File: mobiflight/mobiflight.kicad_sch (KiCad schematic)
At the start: 24 parts, among them J1 Barrel_Jack_Switch, U1 ULN2003, U2 ULN2003, U3 ULN2003, U4 ULN2003, U5 ULN2003, U6 ULN2003

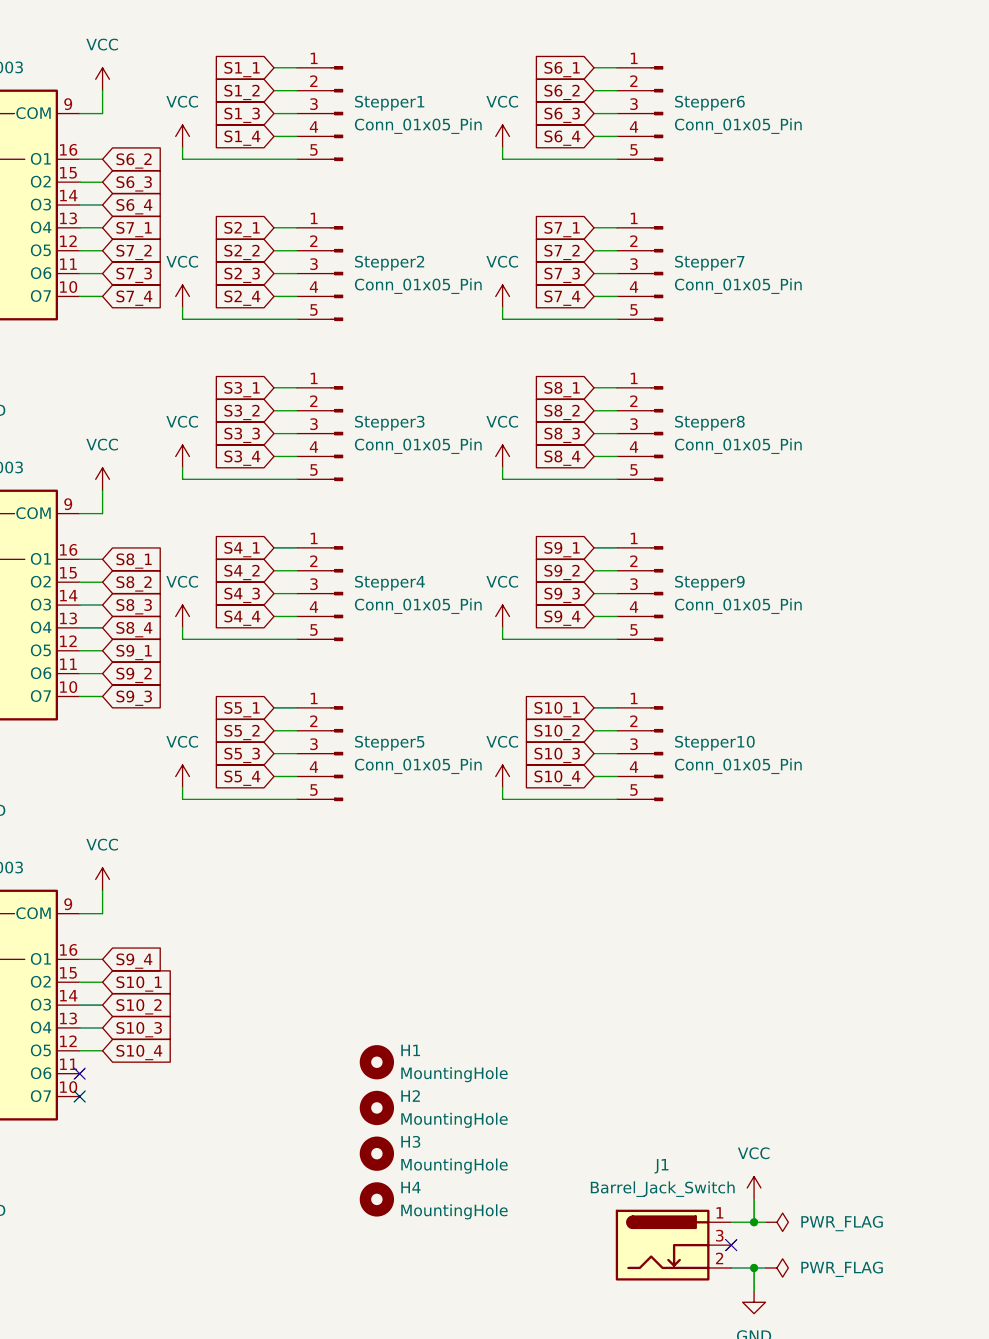
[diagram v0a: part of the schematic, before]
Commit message: add LEDs, move to SMD
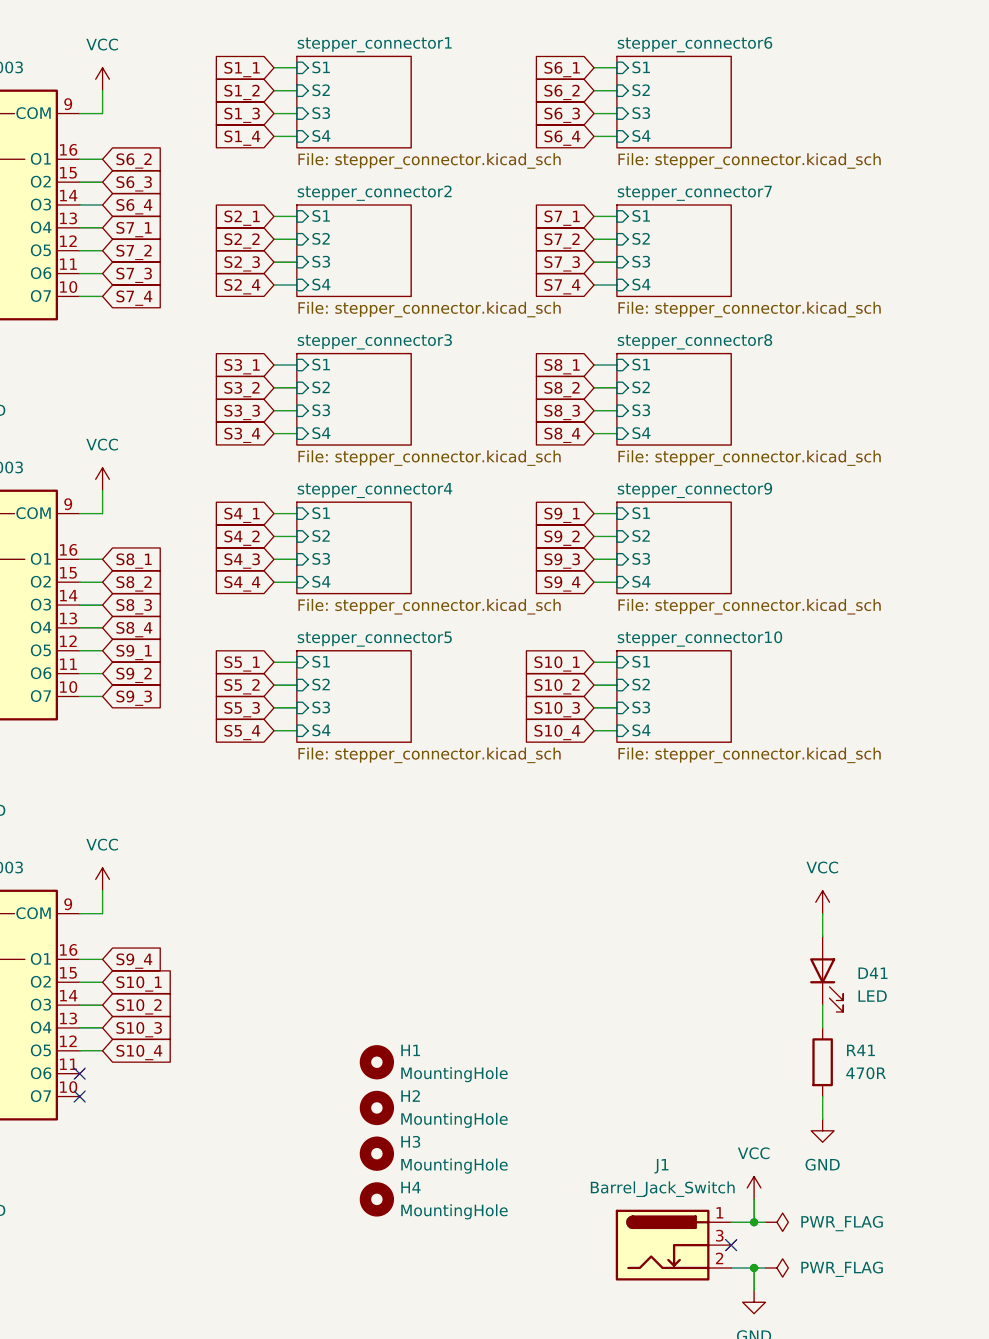
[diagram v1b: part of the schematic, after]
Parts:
- removed Stepper1, Stepper10, Stepper2, Stepper3, Stepper4, Stepper5, Stepper6, Stepper7, Stepper8, Stepper9: Conn_01x05_Pin, Connector_JST:JST_XH_B5B-XH-A_1x05_P2.50mm_Vertical, symbol Connector:Conn_01x05_Pin
- added D41: LED, LED_SMD:LED_0201_0603Metric, symbol Device:LED
- added R41: 470R, Resistor_SMD:R_0201_0603Metric, symbol Device:R
- U1, U2, U3, U4, U5, U6: footprint Package_DIP:DIP-16_W7.62mm_Socket_LongPads -> Package_SO:SOIC-16_3.9x9.9mm_P1.27mm
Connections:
- net GND: now also R41.2
- net VCC: now also D41.2 (A)
- new net: D41.1 (K), R41.1
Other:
- added sheet stepper_connector1 (stepper_connector.kicad_sch)
- added sheet stepper_connector10 (stepper_connector.kicad_sch)
- added sheet stepper_connector2 (stepper_connector.kicad_sch)
- added sheet stepper_connector3 (stepper_connector.kicad_sch)
- added sheet stepper_connector4 (stepper_connector.kicad_sch)
- added sheet stepper_connector5 (stepper_connector.kicad_sch)
- added sheet stepper_connector6 (stepper_connector.kicad_sch)
- added sheet stepper_connector7 (stepper_connector.kicad_sch)
- added sheet stepper_connector8 (stepper_connector.kicad_sch)
- added sheet stepper_connector9 (stepper_connector.kicad_sch)

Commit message: replace components
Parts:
- renumbered D41 to D1, R41 to R1
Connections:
- net D10: now also U1.1 (I1); no longer U1.7 (I7)
- net D11: now also U2.7 (I7); no longer U2.1 (I1)
- net D12: now also U2.6 (I6); no longer U2.2 (I2)
- net D13: now also U2.5 (I5); no longer U2.3 (I3)
- net D15: now also U2.3 (I3); no longer U2.5 (I5)
- net D16: now also U2.2 (I2); no longer U2.6 (I6)
- net D17: now also U2.1 (I1); no longer U2.7 (I7)
- net D18: now also U3.7 (I7); no longer U3.1 (I1)
- net D19: now also U3.6 (I6); no longer U3.2 (I2)
- net D20: now also U3.5 (I5); no longer U3.3 (I3)
- net D22: now also U3.3 (I3); no longer U3.5 (I5)
- net D23: now also U3.2 (I2); no longer U3.6 (I6)
- net D24: now also U3.1 (I1); no longer U3.7 (I7)
- net D25: now also U4.7 (I7); no longer U4.1 (I1)
- net D26: now also U4.6 (I6); no longer U4.2 (I2)
- net D27: now also U4.5 (I5); no longer U4.3 (I3)
- net D29: now also U4.3 (I3); no longer U4.5 (I5)
- net D30: now also U4.2 (I2); no longer U4.6 (I6)
- net D31: now also U4.1 (I1); no longer U4.7 (I7)
- net D4: now also U1.7 (I7); no longer U1.1 (I1)
- net D5: now also U1.6 (I6); no longer U1.2 (I2)
- net D6: now also U1.5 (I5); no longer U1.3 (I3)
- net D8: now also U1.3 (I3); no longer U1.5 (I5)
- net D9: now also U1.2 (I2); no longer U1.6 (I6)
- net S1_1: now also U1.13 (O4); no longer U1.16 (O1)
- net S1_2: now also U1.12 (O5); no longer U1.15 (O2)
- net S1_3: now also U1.11 (O6); no longer U1.14 (O3)
- net S1_4: now also U1.10 (O7); no longer U1.13 (O4)
- net S2_1: now also U2.10 (O7); no longer U1.12 (O5)
- net S2_2: now also U1.16 (O1); no longer U1.11 (O6)
- net S2_3: now also U1.15 (O2); no longer U1.10 (O7)
- net S2_4: now also U1.14 (O3); no longer U2.16 (O1)
- net S3_1: now also U2.14 (O3); no longer U2.15 (O2)
- net S3_2: now also U2.13 (O4); no longer U2.14 (O3)
- net S3_3: now also U2.12 (O5); no longer U2.13 (O4)
- net S3_4: now also U2.11 (O6); no longer U2.12 (O5)
- net S4_1: now also U3.11 (O6); no longer U2.11 (O6)
- net S4_2: now also U3.10 (O7); no longer U2.10 (O7)
- net S4_3: now also U2.16 (O1); no longer U3.16 (O1)
- net S4_4: now also U2.15 (O2); no longer U3.15 (O2)
- net S5_1: now also U3.15 (O2); no longer U3.14 (O3)
- net S5_2: now also U3.14 (O3); no longer U3.13 (O4)
- net S5_3: now also U3.13 (O4); no longer U3.12 (O5)
- net S5_4: now also U3.12 (O5); no longer U3.11 (O6)
- net S6_1: now also U4.12 (O5); no longer U3.10 (O7)
- net S6_2: now also U4.11 (O6); no longer U4.16 (O1)
- net S6_3: now also U4.10 (O7); no longer U4.15 (O2)
- net S6_4: now also U3.16 (O1); no longer U4.14 (O3)
- net S7_1: now also U4.16 (O1); no longer U4.13 (O4)
- net S7_2: now also U4.15 (O2); no longer U4.12 (O5)
- net S7_3: now also U4.14 (O3); no longer U4.11 (O6)
- net S7_4: now also U4.13 (O4); no longer U4.10 (O7)
- net S8_1: now also U5.13 (O4); no longer U5.16 (O1)
- net S8_2: now also U5.14 (O3); no longer U5.15 (O2)
- net S8_3: now also U5.15 (O2); no longer U5.14 (O3)
- net S8_4: now also U5.16 (O1); no longer U5.13 (O4)
- net at A1.D49: no longer Enc2.2 (Pin_2)
- net at A1.D50 (D50_MISO): now also Enc2.2 (Pin_2)
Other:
- moved on the sheet: Enc1

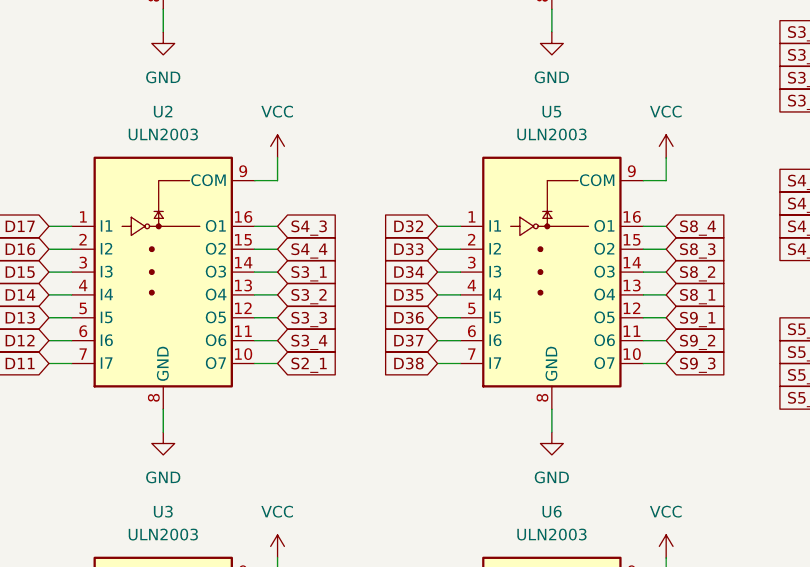
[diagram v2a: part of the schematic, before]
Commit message: wiring for smd mobiflight
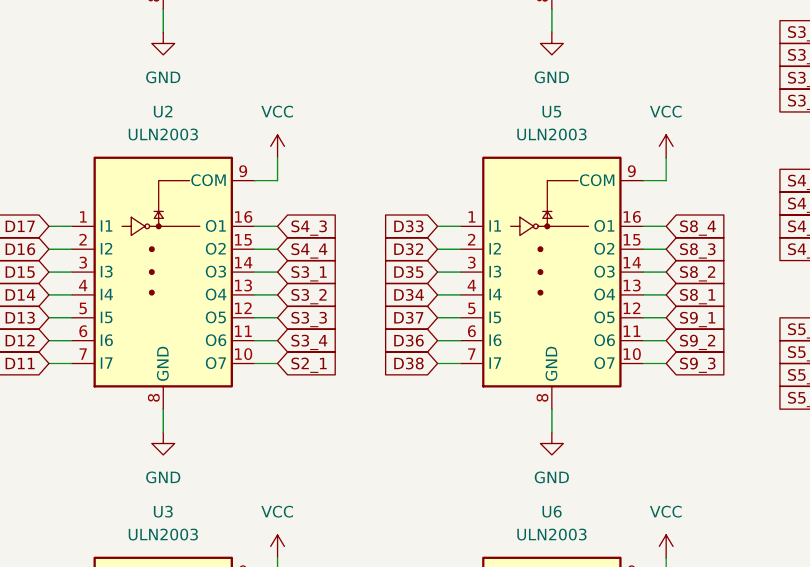
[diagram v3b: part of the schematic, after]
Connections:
- net D32: now also U5.2 (I2); no longer U5.1 (I1)
- net D33: now also U5.1 (I1); no longer U5.2 (I2)
- net D34: now also U5.4 (I4); no longer U5.3 (I3)
- net D35: now also U5.3 (I3); no longer U5.4 (I4)
- net D36: now also U5.6 (I6); no longer U5.5 (I5)
- net D37: now also U5.5 (I5); no longer U5.6 (I6)
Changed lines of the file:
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@@
     )
   )
-  (global_label "D32" (shape input) (at 168.91 73.66 180) (fields_autoplaced)
+  (global_label "D33" (shape input) (at 168.91 73.66 180) (fields_autoplaced)
     (effects (font (size 1.27 1.27)) (justify right))
     (property "Intersheetrefs" "${INTERSHEET_REFS}" (at 162.2358 73.66 0)
@@
     )
   )
-  (global_label "D37" (shape input) (at 168.91 86.36 180) (fields_autoplaced)
+  (global_label "D36" (shape input) (at 168.91 86.36 180) (fields_autoplaced)
     (effects (font (size 1.27 1.27)) (justify right))
     (property "Intersheetrefs" "${INTERSHEET_REFS}" (at 162.2358 86.36 0)
@@
     )
   )
-  (global_label "D33" (shape input) (at 168.91 76.2 180) (fields_autoplaced)
+  (global_label "D32" (shape input) (at 168.91 76.2 180) (fields_autoplaced)
     (effects (font (size 1.27 1.27)) (justify right))
     (property "Intersheetrefs" "${INTERSHEET_REFS}" (at 162.2358 76.2 0)
@@
     )
   )
-  (global_label "D35" (shape input) (at 168.91 81.28 180) (fields_autoplaced)
+  (global_label "D34" (shape input) (at 168.91 81.28 180) (fields_autoplaced)
     (effects (font (size 1.27 1.27)) (justify right))
     (property "Intersheetrefs" "${INTERSHEET_REFS}" (at 162.2358 81.28 0)
@@
     )
   )
-  (global_label "D34" (shape input) (at 168.91 78.74 180) (fields_autoplaced)
+  (global_label "D35" (shape input) (at 168.91 78.74 180) (fields_autoplaced)
     (effects (font (size 1.27 1.27)) (justify right))
     (property "Intersheetrefs" "${INTERSHEET_REFS}" (at 162.2358 78.74 0)
@@
     )
   )
-  (global_label "D36" (shape input) (at 168.91 83.82 180) (fields_autoplaced)
+  (global_label "D37" (shape input) (at 168.91 83.82 180) (fields_autoplaced)
     (effects (font (size 1.27 1.27)) (justify right))
     (property "Intersheetrefs" "${INTERSHEET_REFS}" (at 162.2358 83.82 0)
